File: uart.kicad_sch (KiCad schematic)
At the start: 2 parts, among them U1 MIMX8MM6DVTLZAA, U17 CH343P

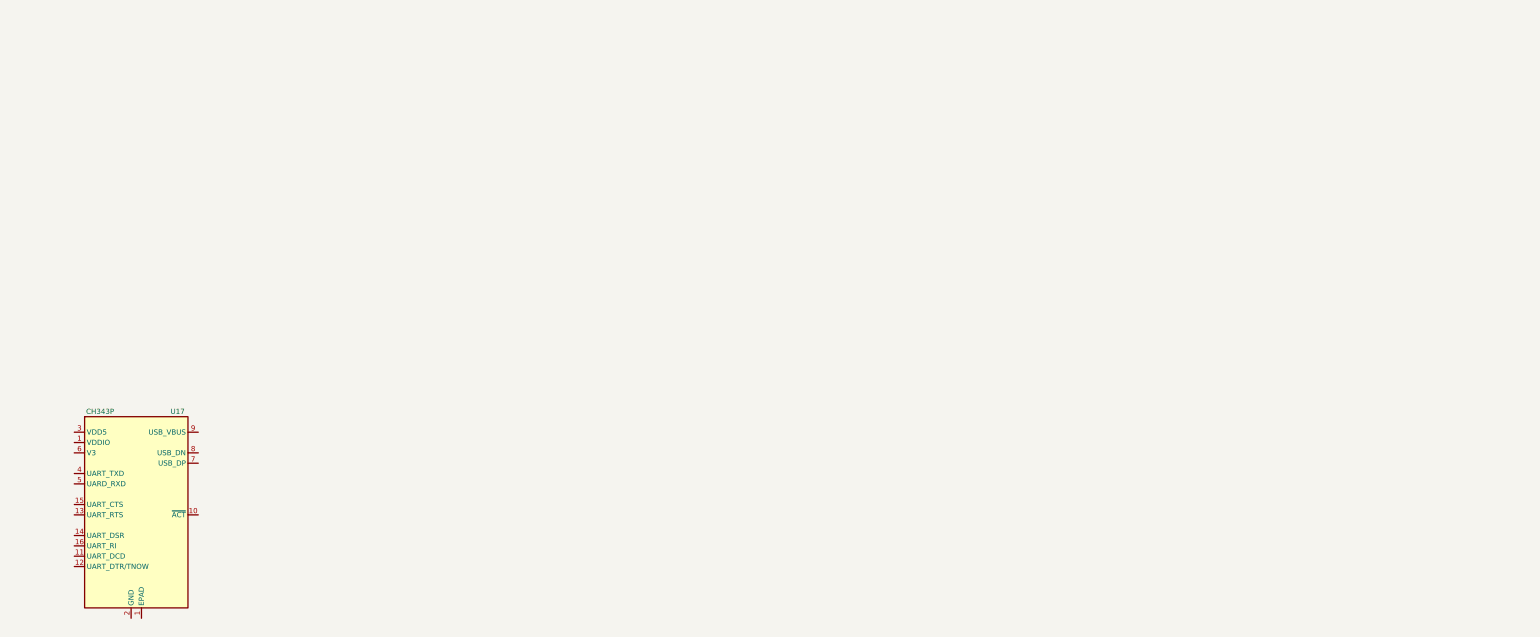
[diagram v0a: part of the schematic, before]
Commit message: enet sch done, other misc sch work
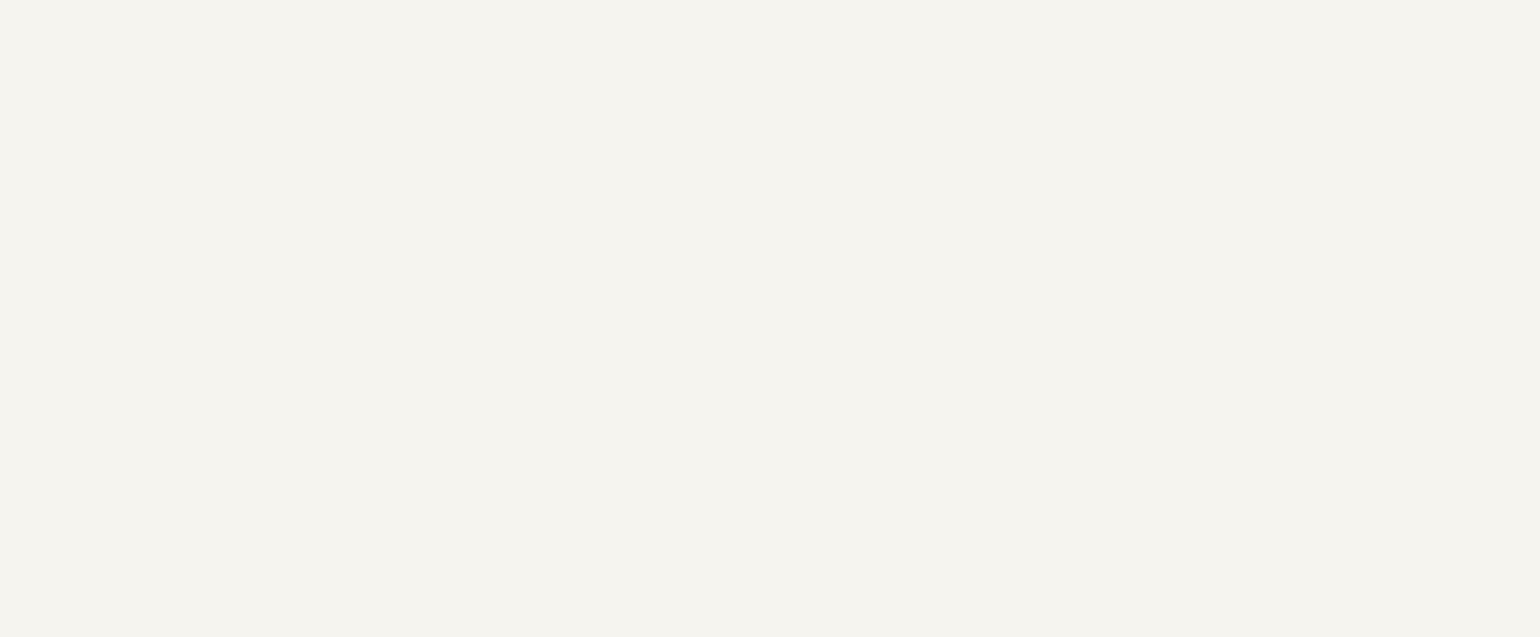
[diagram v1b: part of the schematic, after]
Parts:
- removed U17: CH343P, Package_DFN_QFN:QFN-16-1EP_3x3mm_P0.5mm_EP1.45x1.45mm_ThermalVias, symbol qsbc:CH343P
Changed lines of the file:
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@@
 (kicad_sch (version 20211123) (generator eeschema)
   (paper "A4")
-  (symbol (lib_id "qsbc:CH343P") (at 187.96 69.85 0) (unit 1)
-    (in_bom yes) (on_board yes)
-    (property "Reference" "U17" (id 0) (at 198.12 55.88 0))
-    (property "Value" "CH343P" (id 1) (at 179.07 55.88 0))
-    (property "Footprint" "Package_DFN_QFN:QFN-16-1EP_3x3mm_P0.5mm_EP1.45x1.45mm_ThermalVias" (id 2) (at 226.06 125.73 0)
-      (effects (font (size 1.27 1.27)) hide)
-    )
-    (property "Datasheet" "" (id 3) (at 200.66 57.15 0)
-      (effects (font (size 1.27 1.27)) hide)
-    )
-    (pin "1")
-    (pin "1")
-    (pin "10")
-    (pin "11")
-    (pin "12")
-    (pin "13")
-    (pin "14")
-    (pin "15")
-    (pin "16")
-    (pin "2")
-    (pin "3")
-    (pin "4")
-    (pin "5")
-    (pin "6")
-    (pin "7")
-    (pin "8")
-    (pin "9")
-  )
   (symbol (lib_id "qsbc:MIMX8MM6DVTLZAA") (at 92.71 81.28 0) (unit 15)
     (in_bom yes) (on_board yes) (fields_autoplaced)
